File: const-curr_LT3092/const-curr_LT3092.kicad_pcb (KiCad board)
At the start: 4 copper layers, 26 x 14 mm, 14 parts, among them J1 Conn_01x01, J2 Conn_01x01, J3 Conn_01x01, U1 LT3092xST

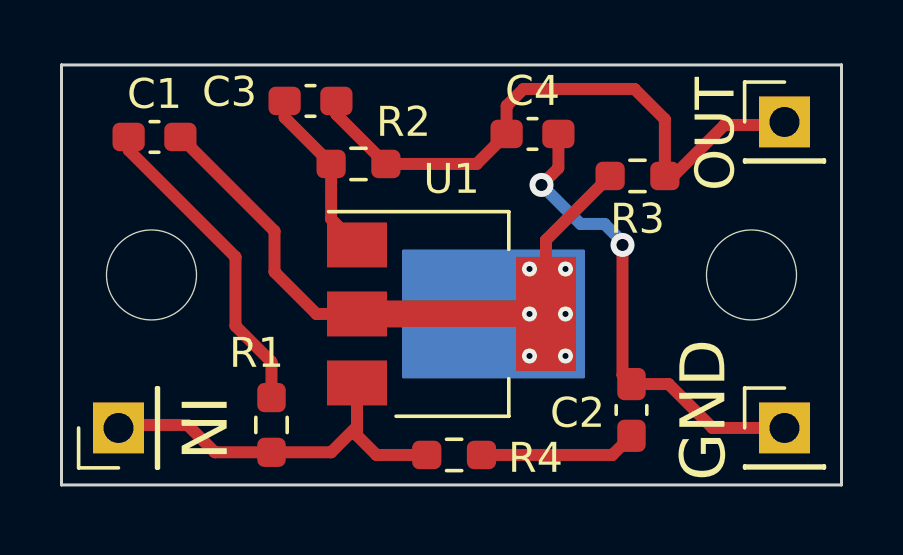
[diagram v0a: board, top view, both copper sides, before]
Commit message: PCB second version.
Size reduced.
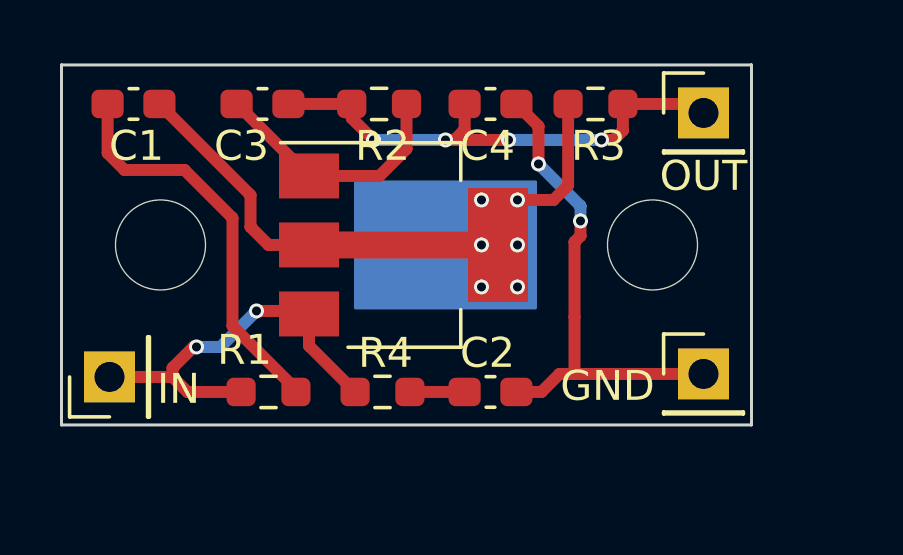
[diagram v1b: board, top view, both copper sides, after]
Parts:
- moved C2 4.74 mm to (95.3, 67.9), turned to 0 degrees
- moved H1 3.45 mm to (100.7, 63.0)
- moved J2 3.24 mm to (102.4, 67.3)
- moved R4 3.18 mm to (91.7, 67.9)
- moved U1 2.80 mm to (92.4, 63.0)
- moved R3 2.78 mm to (98.8, 58.3)
- moved J3 2.72 mm to (102.4, 58.6)
- moved R2 2.11 mm to (91.6, 58.3), turned to 180 degrees
- moved J1 1.73 mm to (82.6, 67.4)
- moved C4 1.72 mm to (95.3, 58.3)
- moved C3 1.60 mm to (87.7, 58.3)
- moved C1 1.30 mm to (83.4, 58.3)
- moved R1 1.10 mm to (87.9, 67.9), turned to 0 degrees
- moved H2 1.04 mm to (84.3, 63.0)
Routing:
- net Net-(C2-Pad1): track 5.26 -> 1.83 mm
- net Net-(C3-Pad2): track 20.6 -> 17.7 mm, vias 0 -> 4
- net Net-(C3-Pad1): track 5.80 -> 8.53 mm
- net Net-(C1-Pad1): track 10.7 -> 13.4 mm
- net Net-(C1-Pad2): track 20.9 -> 19.8 mm
- net Net-(J1-Pad1): track 14.4 -> 13.5 mm, vias 0 -> 2
- net GND: track 16.0 -> 16.7 mm
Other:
- board size 26 x 14 mm -> 23 x 12 mm
